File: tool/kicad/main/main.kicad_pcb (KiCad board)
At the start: 2 copper layers, 115 x 45 mm, 146 parts, among them J1 MICRO-USB-AB, K1 CONN_3, K2 CONN_3, P1 TEST_POINT, P10 TEST_POINT, P11 TEST_POINT, P12 TEST_POINT, P13 TEST_POINT, P14 TEST_POINT, P15 TEST_POINT, P16 TEST_POINT, P17 TEST_POINT, P18 TEST_POINT, P19 TEST_POINT, P2 TEST_POINT, P20 TEST_POINT, P21 TEST_POINT, P22 TEST_POINT, P23 TEST_POINT, P24 TEST_POINT, P25 TEST_POINT, P26 TEST_POINT, P27 TEST_POINT, P28 TEST_POINT, P29 TEST_POINT, P3 TEST_POINT, P30 CONN_3X2, P31 CONN_2, P32 CONN_2, P33 TEST_POINT, P34 TEST_POINT, P35 CONN_6, P37 TEST_POINT, P38 TEST_POINT, P4 TEST_POINT, P5 MIDI-IN, P6 TEST_POINT, P7 TEST_POINT, P8 TEST_POINT, P9 TEST_POINT, U1 SN74LVC2T45, U2 ST-USBLC6-2, U3 EFM32GG332, U4 YM2413, U5 LM386, U6 LM386, U7 ACPL-M21L, X1 48Mhz, X2 CRYSTAL

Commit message: rework main pcb
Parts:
- removed C13, C14, C22, C23: 10uF, pretty:1206
- removed C18, C19: 2.2nF, pretty:0603_S
- removed C20, C21: 1uF, pretty:0603_S
- removed D12: D, pretty:TAIW_SEM_DIODE
- removed K2: CONN_3, pretty:SPC-FD05-3.5mm-stereo-phone-jack
- removed P32: CONN_2, pretty:PIN_1X2_S
- removed P33, P34: TEST_POINT, pretty:Test_Pad_1mm
- removed R37, R39: 10k, pretty:0603_S
- removed R40, R41, R45, R46, R47, R50, R51, R52: 2k2, pretty:0603_S
- removed R43, R44: 4k7/NC, pretty:0603_S
- removed R48, R49: 100, pretty:0603_S
- removed R53, R54: 1k, pretty:0603_S
- removed U5, U6: LM386, pretty:ATMEL_SO8
- removed U7: ACPL-M21L, pretty:SO-5
- added R16: 2k2, pretty:0603_S_R, F.Cu at (154.5, 88.0)
- JP1, JP2, JP3, JP4, JP5: footprint pretty:Solder_Jumper_2mm -> pretty:Solder_Jumper_1.5mm
- P31: value CONN_2 -> CONN_7; footprint pretty:PIN_1X2_S -> pretty:PIN_1X7_S
- P5: value MIDI-IN -> CONN_6; footprint pretty:spiratronics-DIN5-midi -> pretty:PIN_1X6_S
- R1, R10, R11, R12, R13, R14, R17, R18, R19, R2, R20, R21, R22, R23, R24, R25, R26, R27, R28, R3, R31, R32, R34, R35, R36, R38, R4, R42, R5, R6, R7, R8, R9: footprint pretty:0603_S -> pretty:0603_S_R
- R15: value 220 -> 2k2; footprint pretty:0603_S -> pretty:0603_S_R
- moved C1 103.9 mm to (119.2, 85.1)
- moved C10 103.9 mm to (115.2, 85.6)
- moved C11 103.9 mm to (101.2, 85.6)
- moved C12 103.9 mm to (95.2, 90.6)
- moved C15 103.9 mm to (124.8, 102.1)
- moved C16 103.9 mm to (125.0, 107.2)
- moved C17 103.9 mm to (86.0, 85.2)
- moved C2 103.9 mm to (109.0, 103.2)
- moved C24 103.9 mm to (95.2, 93.1)
- moved C3 103.9 mm to (102.2, 96.6)
- moved C4 103.9 mm to (113.0, 85.6)
- moved C5 103.9 mm to (118.2, 95.1)
- moved C6 103.9 mm to (107.5, 85.6)
- moved C7 103.9 mm to (110.7, 82.6)
- moved C8 103.9 mm to (103.2, 85.6)
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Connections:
- P1 pad 1: /XOUT -> /XIN
- P2 pad 1: /XIN -> /XOUT
- P3 pad 1: /XIN3V3 -> /XOUT3V3
- P31 pad 1: /ROI -> GND
- P31 pad 2: Net-(C13-Pad1) -> +3.3V
- P4 pad 1: /XOUT3V3 -> /XIN3V3
- P5 pad 1: Net-(P5-Pad1) -> GND
- P5 pad 2: Net-(P5-Pad2) -> +3.3V
- P5 pad 3: Net-(P5-Pad3) -> +5V
- P5 pad 4: Net-(P5-Pad4) -> /MIDI_IN
- P5 pad 5: Net-(D12-Pad1) -> /MO
- P5 pad 6: (no net) -> /RO
- R15 pad 1: Net-(D12-Pad2) -> GND
- R15 pad 2: Net-(P5-Pad4) -> /MO
- U1 pad 2: /XOUT3V3 -> /XIN3V3
- U1 pad 3: /XIN3V3 -> /XOUT3V3
- U1 pad 6: /XIN -> /XOUT
- U1 pad 7: /XOUT -> /XIN
- U3 pad 1: /XIN3V3 -> /XOUT3V3
- U3 pad 2: /XOUT3V3 -> /XIN3V3
- U3 pad 28: /ROd2 -> /RO_SAMPLE
- U3 pad 29: /MOd2 -> /MO_SAMPLE
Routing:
- net /RO_SAMPLE: track 0.00 -> 89.4 mm, vias 0 -> 5
- net /MO_SAMPLE: track 0.00 -> 89.3 mm, vias 0 -> 5
- net /MOd2: track 87.0 -> 0.00 mm, vias 6 -> 0
- net /ROd2: track 76.8 -> 0.00 mm, vias 6 -> 0
- net /ROI: track 41.1 -> 0.00 mm
- net /MO: track 8.84 -> 37.3 mm, vias 0 -> 1
- net /RO: track 8.56 -> 33.2 mm
- net GND: track 77.3 -> 54.0 mm, vias 44 -> 35
- net /MOI: track 17.5 -> 0.00 mm
- net Net-(D12-Pad1): track 15.7 -> 0.00 mm
- net /MOA: track 15.6 -> 0.00 mm
- net +5V: track 94.1 -> 105.7 mm, vias 8 -> 10
- net /ROA3: track 9.09 -> 0.00 mm
- net /MOA3: track 9.07 -> 0.00 mm
- net Net-(P5-Pad4): track 7.94 -> 0.00 mm
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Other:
- board size 115 x 45 mm -> 81.7 x 45 mm
- board text added: "v1"
- board text removed: "55cd0132cc25ed18f8d705411f72c79030af9bd8"
- board text removed: "v0"

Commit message: main board WIP
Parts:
- removed P1, P11, P12, P13, P14, P15, P16, P17, P18, P19, P2, P20, P21, P22, P23, P24, P25, P26, P3, P4, P6, P7, P8, P9: TEST_POINT, pretty:Test_Pad_1mm
- moved R32 22.9 mm to (126.5, 96.2), turned to 270 degrees
- moved C15 20.8 mm to (144.8, 107.8), turned to 270 degrees
- moved R34 18.5 mm to (126.5, 99.5)
- moved JP2 17.9 mm to (129.2, 96.8), turned to 180 degrees
- moved JP3 14.1 mm to (129.2, 99.0), turned to 180 degrees
- moved R20 10.8 mm to (129.0, 89.8)
- moved P31 10.7 mm to (154.0, 102.0)
- moved R24 10.3 mm to (129.0, 88.0)
- moved R19 9.78 mm to (129.0, 86.2)
- moved P5 9.50 mm to (154.0, 83.0)
- moved R23 9.31 mm to (129.0, 84.5)
- moved R18 8.88 mm to (129.0, 82.8)
- moved X2 8.67 mm to (137.8, 107.0), turned to 0 degrees
- moved R22 8.48 mm to (129.0, 81.0)
- moved JP1 8.41 mm to (132.2, 102.1)
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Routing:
- net +3.3V: track 140.2 -> 0.00 mm, vias 12 -> 0
- net +5V: track 105.7 -> 0.00 mm, vias 10 -> 0
- net /MIDI_IN: track 92.9 -> 0.00 mm, vias 3 -> 0
- net /~IC: track 92.2 -> 0.00 mm, vias 2 -> 0
- net /RO_SAMPLE: track 89.4 -> 0.00 mm, vias 5 -> 0
- net /MO_SAMPLE: track 89.3 -> 0.00 mm, vias 5 -> 0
- net /~CS: track 89.1 -> 0.00 mm, vias 2 -> 0
- net /~WE: track 87.9 -> 0.00 mm, vias 2 -> 0
- net /A0: track 85.0 -> 0.00 mm, vias 2 -> 0
- net /D0: track 54.8 -> 0.00 mm, vias 2 -> 0
- net /D1: track 54.5 -> 0.00 mm
- net GND: track 54.0 -> 0.00 mm, vias 35 -> 0
- net /SWC: track 53.6 -> 0.00 mm, vias 2 -> 0
- net /~RESET: track 50.5 -> 0.00 mm, vias 4 -> 0
- net /D7: track 40.8 -> 0.00 mm, vias 2 -> 0
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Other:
- board size 81.7 x 45 mm -> 71.9 x 39.3 mm

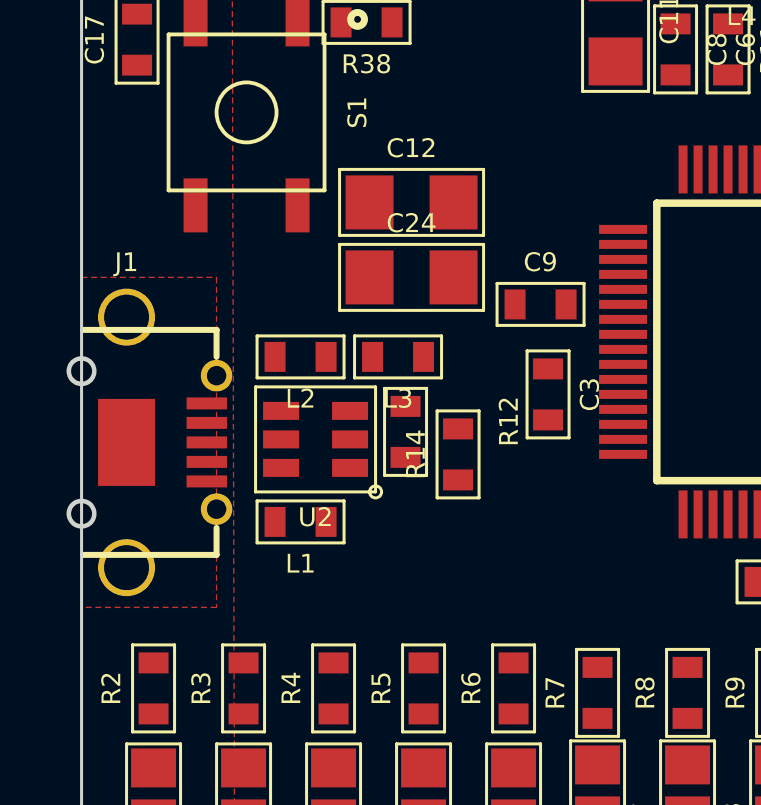
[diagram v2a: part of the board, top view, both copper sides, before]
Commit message: use new prefered USB-B connector
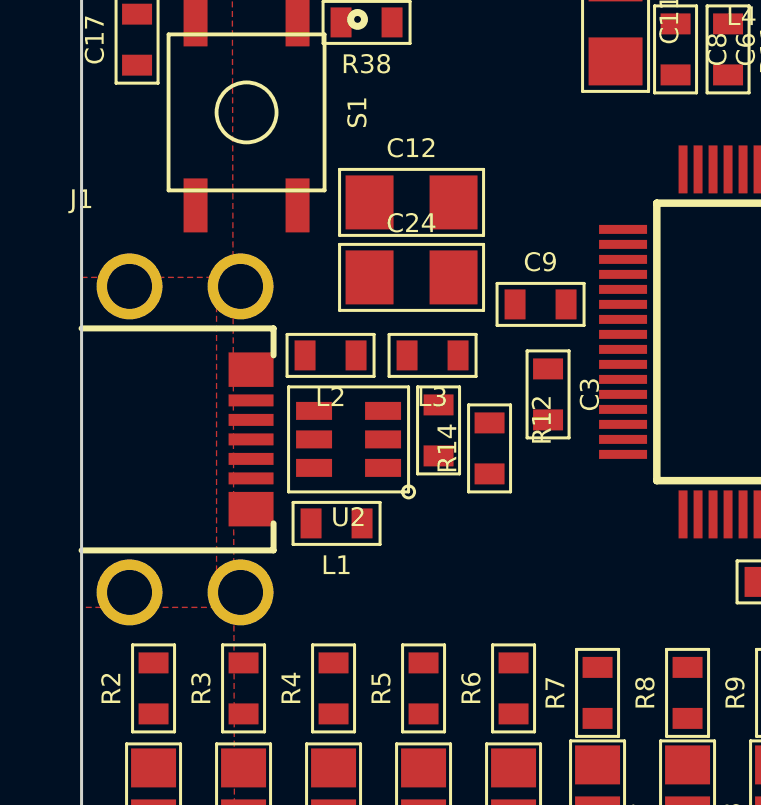
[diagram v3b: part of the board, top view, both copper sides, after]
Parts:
- J1: footprint pretty:USB-MICRO-AB-Molex-47590-0001 -> pretty:USB-MICRO-B-FCI-10103593-0001LF
- moved J1 1.50 mm to (84.2, 98.5)
- moved L1 1.20 mm to (92.7, 101.3)
- moved L3 1.15 mm to (95.9, 95.7)
- moved R12 1.10 mm to (96.1, 98.2)
- moved U2 1.10 mm to (93.1, 98.5)
- moved R14 1.07 mm to (97.8, 98.8)
- moved L2 1.00 mm to (92.5, 95.7)
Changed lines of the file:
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@@
   (general
     (links 190)
-    (no_connects 162)
-    (area 76.328601 73.549999 156.150001 113.100001)
+    (no_connects 164)
+    (area 84.149999 73.549999 156.150001 112.950001)
     (thickness 1.6)
     (drawings 14)
@@
     (add_net /~WE)
     (add_net /~WE')
-    (add_net "Net-(C14-Pad1)")
     (add_net "Net-(C15-Pad1)")
     (add_net "Net-(C16-Pad1)")
-    (add_net "Net-(C21-Pad1)")
     (add_net "Net-(D1-Pad1)")
     (add_net "Net-(D10-Pad1)")
     (add_net "Net-(D11-Pad1)")
-    (add_net "Net-(D12-Pad2)")
     (add_net "Net-(D2-Pad1)")
     (add_net "Net-(D3-Pad1)")
@@
       (net 68 GND))
   )
-  (module pretty:USB-MICRO-AB-Molex-47590-0001 (layer F.Cu)
-    (at 85.7 98.6)
-    (descr "USB-MICRO-AB-Molex-47590-0001 RS 702-5481")
-    (fp_text reference J1 (at 0 -6) (layer F.SilkS)
-      (effects (font (size 0.625 0.625) (thickness 0.1)))
-    )
-    (fp_text value MICRO-USB-AB (at 0 0) (layer F.SilkS) hide
-      (effects (font (thickness 0.15)))
-    )
-    (fp_line (start -1.45 4.75) (end -1.45 -4.75) (layer Dwgs.User) (width 0.2))
-    (fp_line (start -1.45 -3.75) (end -2.2 -3.75) (layer Dwgs.User) (width 0.2))
-    (fp_line (start -1.45 3.75) (end -2.2 3.75) (layer Dwgs.User) (width 0.2))
-    (fp_line (start -2.2 3.75) (end -2.2 -3.75) (layer Dwgs.User) (width 0.2))
-    (fp_line (start -1.45 -3.75) (end 3 -3.75) (layer F.SilkS) (width 0.2))
-    (fp_line (start -1.45 3.75) (end 3 3.75) (layer F.SilkS) (width 0.2))
-    (fp_line (start 3 -3.75) (end 3 -2.85) (layer F.SilkS) (width 0.2))
-    (fp_line (start 3 3.75) (end 3 2.85) (layer F.SilkS) (width 0.2))
-    (fp_circle (center -1.5 -2.375) (end -1.19948 -2.07448) (layer Edge.Cuts) (width 0.15))
-    (fp_circle (center -1.5 2.375) (end -1.19948 2.67552) (layer Edge.Cuts) (width 0.15))
-    (pad 6 thru_hole circle (at 3 -2.225) (size 1.05 1.05) (drill 0.65) (layers *.Cu *.Mask F.SilkS)
-      (net 31 /GI_2))
-    (pad 7 thru_hole circle (at 3 2.225 180) (size 1.05 1.05) (drill 0.65) (layers *.Cu *.Mask F.SilkS)
-      (net 31 /GI_2))
-    (pad 8 thru_hole circle (at 0 4.175) (size 1.9 1.9) (drill 1.5) (layers *.Cu *.Mask F.SilkS)
-      (net 31 /GI_2))
-    (pad 9 thru_hole circle (at 0 -4.175 180) (size 1.9 1.9) (drill 1.5) (layers *.Cu *.Mask F.SilkS)
-      (net 31 /GI_2))
-    (pad 10 smd rect (at 0 0) (size 1.9 2.9) (layers F.Cu F.Paste F.Mask)
-      (net 31 /GI_2))
-    (pad 1 smd rect (at 2.675 1.3 180) (size 1.35 0.4) (layers F.Cu F.Paste F.Mask)
-      (net 51 /VBUS_IN))
-    (pad 2 smd rect (at 2.675 0.65 180) (size 1.35 0.4) (layers F.Cu F.Paste F.Mask)
-      (net 11 /D-_IN))
-    (pad 3 smd rect (at 2.675 0 180) (size 1.35 0.4) (layers F.Cu F.Paste F.Mask)
-      (net 8 /D+_IN))
-    (pad 4 smd rect (at 2.675 -0.65 180) (size 1.35 0.4) (layers F.Cu F.Paste F.Mask)
-      (net 82 "Net-(J1-Pad4)"))
-    (pad 5 smd rect (at 2.675 -1.3 180) (size 1.35 0.4) (layers F.Cu F.Paste F.Mask)
-      (net 32 /G_I1))
-  )
   (module pretty:PIN_1X3 (layer F.Cu)
     (at 120.2 76.1 90)
@@
   )
   (module pretty:0603_S (layer F.Cu)
-    (at 91.5 101.25 180)
+    (at 92.7 101.3 180)
     (descr "Generic 0603 footprint made slightly smaller for more densely populated boards used for resistor and capacitor")
     (fp_text reference L1 (at 0 -1.4 180) (layer F.SilkS)
@@
   )
   (module pretty:0603_S (layer F.Cu)
-    (at 91.5 95.75 180)
+    (at 92.5 95.7 180)
     (descr "Generic 0603 footprint made slightly smaller for more densely populated boards used for resistor and capacitor")
     (fp_text reference L2 (at 0 -1.4 180) (layer F.SilkS)
@@
   )
   (module pretty:0603_S (layer F.Cu)
-    (at 94.75 95.75 180)
+    (at 95.9 95.7 180)
     (descr "Generic 0603 footprint made slightly smaller for more densely populated boards used for resistor and capacitor")
     (fp_text reference L3 (at 0 -1.4 180) (layer F.SilkS)
@@
   )
   (module pretty:SOT-23-6L (layer F.Cu)
-    (at 92 98.5 180)
+    (at 93.1 98.5 180)
     (descr "generic SOT-23-6L footprint")
     (fp_text reference U2 (at 0 -2.6 180) (layer F.SilkS)
@@
   )
   (module pretty:0603_S_R (layer F.Cu)
-    (at 95 98.25 270)
+    (at 96.1 98.2 270)
     (descr "Generic 0603 footprint made slightly smaller for more densely populated boards used for resistor and capacitor")
     (fp_text reference R12 (at -0.35 -3.45 270) (layer F.SilkS)
@@
   )
   (module pretty:0603_S_R (layer F.Cu)
-    (at 96.75 99 90)
+    (at 97.8 98.8 90)
     (descr "Generic 0603 footprint made slightly smaller for more densely populated boards used for resistor and capacitor")
     (fp_text reference R14 (at 0 -1.4 90) (layer F.SilkS)
@@
       (net 56 /XOUT'))
   )
+  (module pretty:USB-MICRO-B-FCI-10103593-0001LF (layer F.Cu)
+    (at 84.2 98.5)
+    (descr "RS 714-2338")
+    (fp_text reference J1 (at 0 -8) (layer F.SilkS)
+      (effects (font (size 0.625 0.625) (thickness 0.1)))
+    )
+    (fp_text value MICRO-USB-AB (at 0 0) (layer F.SilkS) hide
+      (effects (font (thickness 0.15)))
+    )
+    (fp_line (start 0 4.7) (end 0 -4.7) (layer Dwgs.User) (width 0.2))
+    (fp_line (start 0 -3.7) (end -0.62 -3.7) (layer Dwgs.User) (width 0.2))
+    (fp_line (start 0 3.7) (end -0.62 3.7) (layer Dwgs.User) (width 0.2))
+    (fp_line (start -0.62 3.7) (end -0.62 -3.7) (layer Dwgs.User) (width 0.2))
+    (fp_line (start 0 -3.7) (end 6.4 -3.7) (layer F.SilkS) (width 0.2))
+    (fp_line (start 0 3.7) (end 6.4 3.7) (layer F.SilkS) (width 0.2))
+    (fp_line (start 6.4 -3.7) (end 6.4 -2.8) (layer F.SilkS) (width 0.2))
+    (fp_line (start 6.4 3.7) (end 6.4 2.8) (layer F.SilkS) (width 0.2))
+    (pad 10 thru_hole circle (at 5.3 5.1) (size 2.2 2.2) (drill 1.5) (layers *.Cu *.Mask)
+      (net 31 /GI_2))
+    (pad 11 thru_hole circle (at 5.3 -5.1 180) (size 2.2 2.2) (drill 1.5) (layers *.Cu *.Mask))
+    (pad 8 thru_hole circle (at 1.6 5.1) (size 2.2 2.2) (drill 1.5) (layers *.Cu *.Mask)
+      (net 31 /GI_2))
+    (pad 9 thru_hole circle (at 1.6 -5.1 180) (size 2.2 2.2) (drill 1.5) (layers *.Cu *.Mask)
+      (net 31 /GI_2))
+    (pad 1 smd rect (at 5.65 1.3 180) (size 1.5 0.4) (layers F.Cu F.Paste F.Mask)
+      (net 51 /VBUS_IN))
+    (pad 2 smd rect (at 5.65 0.65 180) (size 1.5 0.4) (layers F.Cu F.Paste F.Mask)
+      (net 11 /D-_IN))
+    (pad 3 smd rect (at 5.65 0 180) (size 1.5 0.4) (layers F.Cu F.Paste F.Mask)
+      (net 8 /D+_IN))
+    (pad 4 smd rect (at 5.65 -0.65 180) (size 1.5 0.4) (layers F.Cu F.Paste F.Mask)
+      (net 82 "Net-(J1-Pad4)"))
+    (pad 5 smd rect (at 5.65 -1.3 180) (size 1.5 0.4) (layers F.Cu F.Paste F.Mask)
+      (net 32 /G_I1))
+    (pad 6 smd rect (at 5.65 -2.325) (size 1.5 1.15) (layers F.Cu F.Paste F.Mask)
+      (net 31 /GI_2))
+    (pad 7 smd rect (at 5.65 2.325) (size 1.5 1.15) (layers F.Cu F.Paste F.Mask)
+      (net 31 /GI_2))
+  )
   (gr_line (start 154.1 73.6) (end 86.2 73.6) (angle 90) (layer Edge.Cuts) (width 0.1))

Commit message: main layout (WIP)
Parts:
- moved C1 18.2 mm to (101.3, 88.3)
- moved C10 2.90 mm to (112.3, 85.5)
- moved C11 1.90 mm to (100.1, 84.5)
- moved C4 1.90 mm to (110.6, 85.5)
- moved C6 1.90 mm to (105.8, 85.5)
- moved C7 1.90 mm to (108.8, 82.6)
- moved C8 1.90 mm to (102.1, 85.5)
- moved L4 1.90 mm to (104.3, 82.6)
- moved R11 1.90 mm to (103.8, 85.5)
- moved X1 1.90 mm to (108.3, 85.6)
- moved C9 0.61 mm to (99.4, 94.6)
- moved R14 0.41 mm to (97.9, 99.2)
- moved C5 0.36 mm to (116.4, 95.1)
- moved L1 0.10 mm to (92.6, 101.3)
- moved L2 0.10 mm to (92.6, 95.7)
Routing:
- net +3.3V: track 0.00 -> 107.0 mm, vias 0 -> 6
- net GND: track 0.00 -> 56.6 mm, vias 0 -> 29
- net /~RESET: track 0.00 -> 54.9 mm, vias 0 -> 1
- net /D1: track 0.00 -> 49.2 mm
- net /D0: track 0.00 -> 47.4 mm
- net /MO: track 0.00 -> 37.0 mm
- net /D6: track 0.00 -> 28.2 mm, vias 0 -> 2
- net /D3: track 0.00 -> 27.7 mm
- net /D7: track 0.00 -> 27.7 mm, vias 0 -> 2
- net /RO: track 0.00 -> 26.6 mm, vias 0 -> 1
- net /DEBUG_TX: track 0.00 -> 25.9 mm
- net /GI_2: track 0.00 -> 24.1 mm
- net /SWC: track 0.00 -> 22.2 mm, vias 0 -> 1
- net /DEBUG_RX: track 0.00 -> 20.4 mm
- net /D2: track 0.00 -> 20.1 mm
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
